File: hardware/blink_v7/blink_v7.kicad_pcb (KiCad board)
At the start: 2 copper layers, 119 x 92 mm, 78 parts, among them J1 Conn_01x02, J10 Conn_01x04_Pin, J11 KH-BNC50-3511, J12 KH-BNC50-3511, J13 KH-BNC50-3511, J14 Conn_02x16_Odd_Even, J2 PJ-320D, J3 PJ-320D, J4 KH-BNC50-3511, J5 Conn_01x04_Pin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

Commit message: update pages to v7
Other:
- board text added: "Blink Rev 7.0 Cullen Jennings 2023"
- board text removed: "Blink Rev 6.0 Cullen Jennings Sept 2023"
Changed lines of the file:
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@@
     (thickness 1.6)
   )
-  (paper "A4")
+  (paper "USLetter")
   (title_block
-    (title "Blinky V4")
+    (title "Blink V7")
     (date "2023-07-04")
     (company "Cullen Jennings")
@@
   (gr_line (start 111 38) (end 111 130)
     (stroke (width 0.1) (type default)) (layer "Edge.Cuts"))
-  (gr_text "Blink Rev 6.0 Cullen Jennings Sept 2023" (at 176.739349 127.829283) (layer "F.SilkS")
+  (gr_text "Blink Rev 7.0 Cullen Jennings 2023" (at 176.739349 127.829283) (layer "F.SilkS")
     (effects (font (size 1 1) (thickness 0.15)) (justify left bottom))
   )

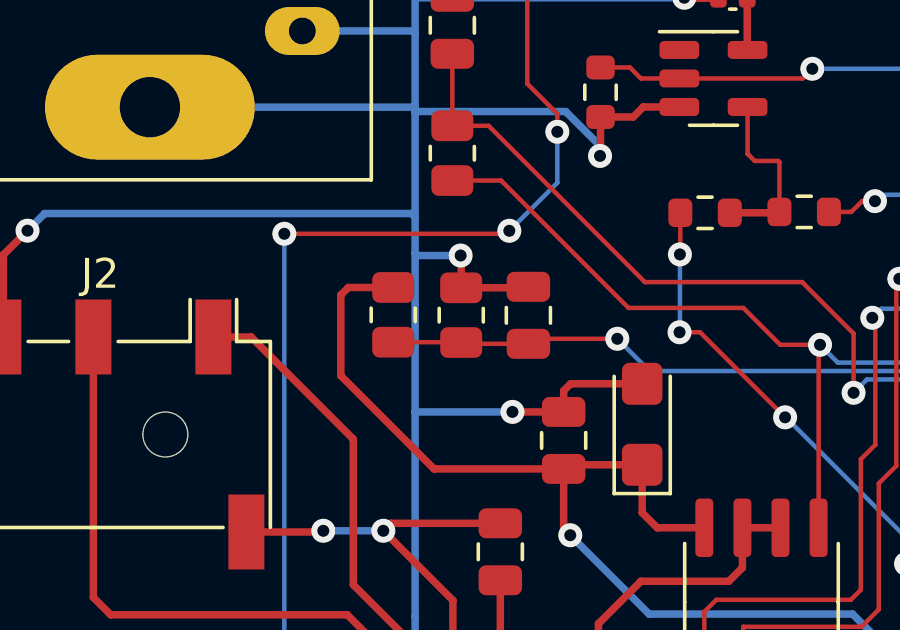
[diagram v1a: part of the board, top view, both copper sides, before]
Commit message: change output gain of audio out by -20dB
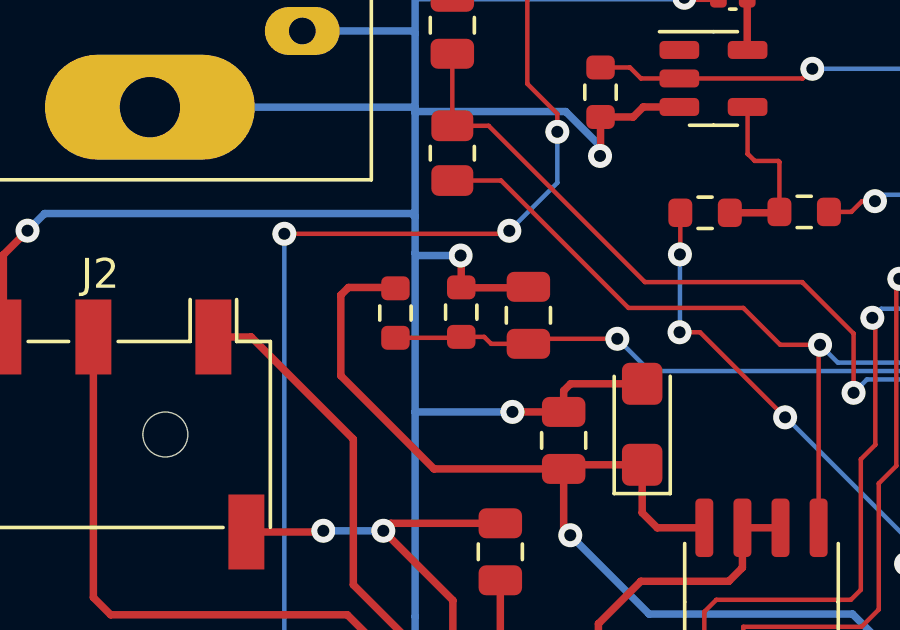
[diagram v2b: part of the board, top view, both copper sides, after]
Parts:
- R10, R11: value 47k -> 1K0; footprint Resistor_SMD:R_0805_2012Metric -> Resistor_SMD:R_0603_1608Metric
- R7: value 10R -> 1R0
- moved R11 0.10 mm to (129.3, 63.9), turned to 90 degrees
- moved R10 0.10 mm to (127.1, 63.9), turned to -90 degrees
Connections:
- R10 pad 1: Net-(J10-Pin_4) -> +3.3VA
- R10 pad 2: +3.3VA -> Net-(J10-Pin_4)
- R11 pad 1: GND -> Net-(J10-Pin_4)
- R11 pad 2: Net-(J10-Pin_4) -> GND

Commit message: route usb
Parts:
- removed C2: 10uF, Capacitor_Tantalum_SMD:CP_EIA-3216-18_Kemet-A
- added C27: 100n, Capacitor_SMD:C_0402_1005Metric, F.Cu at (205.6, 75.6)
- added C28: 4u7, Capacitor_SMD:C_0402_1005Metric, F.Cu at (213.3, 62.2)
- added C29: 4u7, Capacitor_SMD:C_0402_1005Metric, F.Cu at (181.8, 105.9)
- added D1: LED, LED_SMD:LED_0805_2012Metric, F.Cu at (208.4, 53.9)
- added D2: 1N5819WS, Diode_SMD:D_SOD-323, F.Cu at (191.6, 106.4)
- added D3: 1N5819WS, Diode_SMD:D_SOD-323, F.Cu at (194.1, 106.3)
- added J9: USB_C_Receptacle, Connector_USB:USB_C_Receptacle_HRO_TYPE-C-31-M-12, F.Cu at (226.0, 66.0)
- added R21: 5k1, Resistor_SMD:R_0402_1005Metric, F.Cu at (217.2, 63.9)
- added R22: 5k1, Resistor_SMD:R_0402_1005Metric, F.Cu at (217.0, 70.4)
- added R27: 1K0, Resistor_SMD:R_0603_1608Metric, F.Cu at (192.2, 54.0)
- added R30: 2K0, Resistor_SMD:R_0603_1608Metric, F.Cu at (203.6, 55.1)
- added SW1: SW_SPST, Button_Switch_THT:SW_SPST_Omron_B3F-315x_Angled, F.Cu at (227.3, 117.2)
- added U7: CH340C, Package_SO:SOIC-16_3.9x9.9mm_P1.27mm, F.Cu at (207.5, 68.8)
- added U8: USBLC6-2P6, Package_TO_SOT_SMD:SOT-666, F.Cu at (216.3, 66.4)
- added U9: MCP73832-2-OT, Package_TO_SOT_SMD:SOT-23-5, F.Cu at (197.6, 55.4)
- R5: value 1K -> 1K0
- moved J4 0.15 mm to (219.7, 51.0)
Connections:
- C1 pad 2: +6V -> Net-(SW1-B)
- J1 pad 2: +6V -> +BATT
- U1 pad 3: +6V -> Net-(SW1-B)
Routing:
- net +6V: track 146.0 -> 0.00 mm
- net VBUS: track 0.00 -> 103.2 mm, vias 0 -> 5
- net Net-(SW1-B): track 0.00 -> 100.8 mm
- net GND: track 826.1 -> 906.9 mm, vias 34 -> 42
- net +BATT: track 0.00 -> 78.8 mm, vias 0 -> 2
- net /USB_TX: track 47.7 -> 115.1 mm, vias 2 -> 4
- net +3.3V: track 370.2 -> 422.0 mm, vias 15 -> 16
- net Net-(D2-K): track 0.00 -> 50.2 mm
- net /USB_RX: track 67.9 -> 116.1 mm, vias 4 -> 5
- net Net-(D1-K): track 0.00 -> 19.2 mm
- net unconnected-(J9-SHIELD-PadS1): track 0.00 -> 17.0 mm
- net Net-(J9-D--PadA7): track 0.00 -> 13.4 mm
- net Net-(J9-D+-PadA6): track 0.00 -> 8.93 mm
- net Net-(U7-UD+): track 0.00 -> 6.93 mm
- net Net-(J9-CC1): track 0.00 -> 6.40 mm
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
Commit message: pcb
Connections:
- J14 pad 2: +6V -> +BATT
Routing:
- net +BATT: track 78.8 -> 124.5 mm
- net +3.3V: track 422.0 -> 427.3 mm
- net Net-(J12-In): track 51.1 -> 49.9 mm
- net /USB_TX: track 115.1 -> 114.5 mm

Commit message: added new power switch
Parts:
- SW1: value SW_SPST -> MK-12C02-G025; footprint Button_Switch_THT:SW_SPST_Omron_B3F-315x_Angled -> blinky_footprints:MK-12C02-G025
- moved SW1 2.11 mm to (227.9, 119.3), turned to 90 degrees
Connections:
- SW1 pad 1: Net-(D2-K) -> unconnected-(SW1-Pad1)
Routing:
- net Net-(D2-K): track 50.2 -> 54.4 mm
- net Net-(U1-VI): track 100.8 -> 99.6 mm

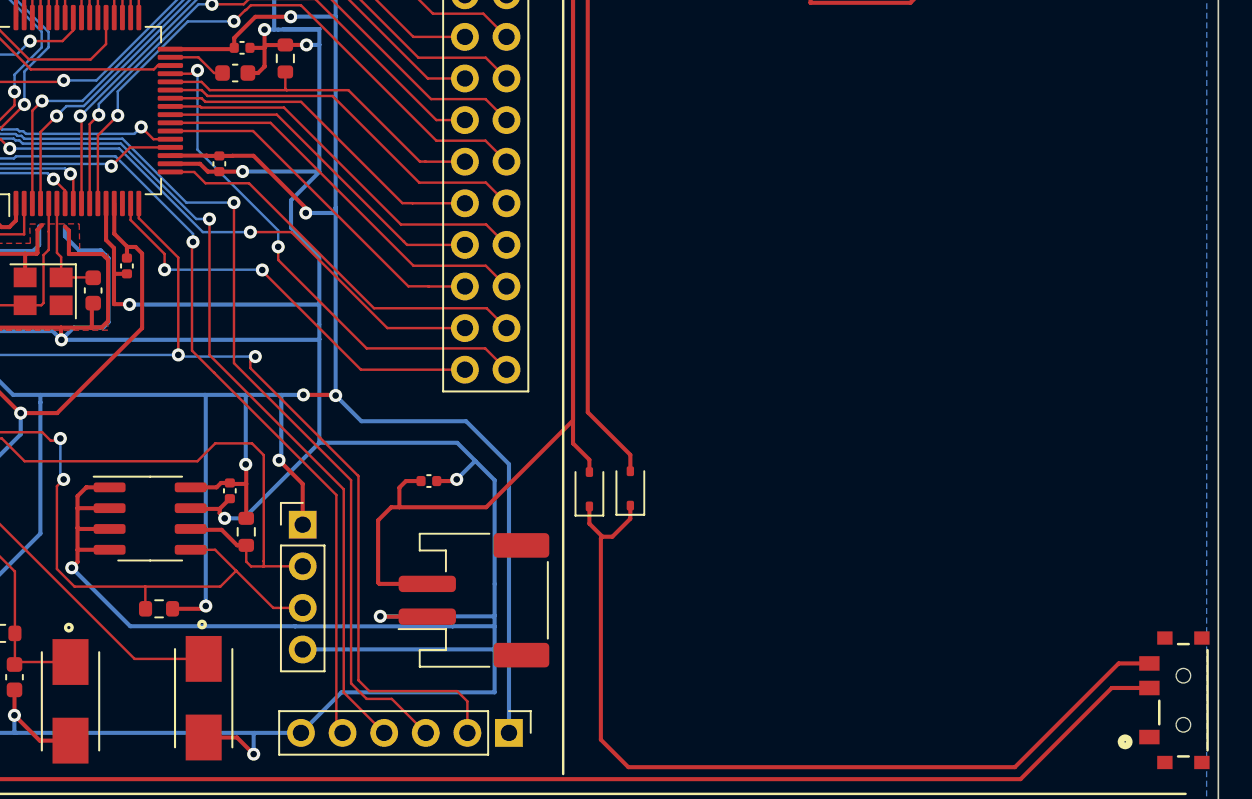
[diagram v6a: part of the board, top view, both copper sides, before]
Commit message: start to add push button switch
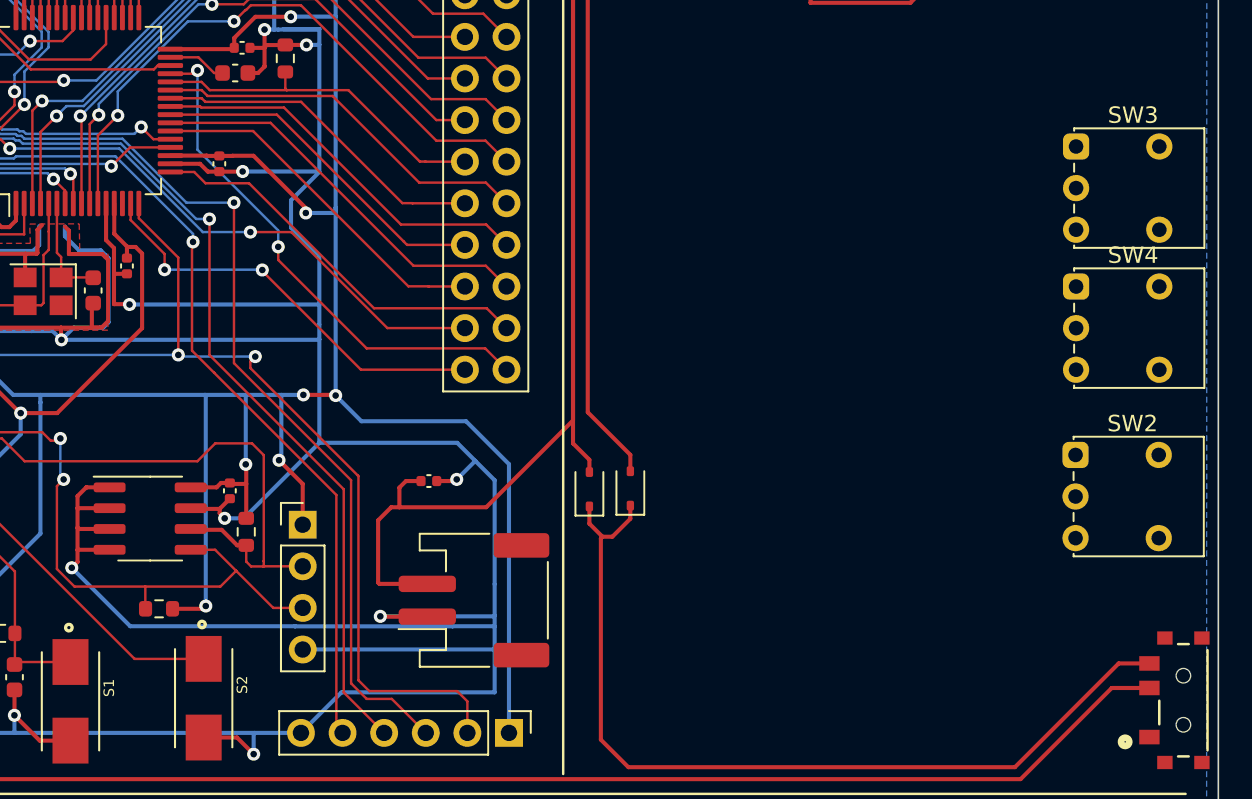
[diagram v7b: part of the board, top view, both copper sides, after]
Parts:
- added SW2: SW_SPDT, Button_Switch_THT:SW_Push_1P2T_Vertical_E-Switch_800UDP8P1A1M6, F.Cu at (221.3, 104.3)
- added SW3: SW_SPDT, Button_Switch_THT:SW_Push_1P2T_Vertical_E-Switch_800UDP8P1A1M6, F.Cu at (221.3, 85.5)
- added SW4: SW_SPDT, Button_Switch_THT:SW_Push_1P2T_Vertical_E-Switch_800UDP8P1A1M6, F.Cu at (221.3, 94.0)
